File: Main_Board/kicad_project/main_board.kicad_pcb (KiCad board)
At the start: 4 copper layers, 150 x 150 mm, 237 parts, among them J1 MOTOR, J10 USB_B_Micro, J11 DATA_UART, J12 I2C_EXTERNAL, J13 DEBUG_HEADER, J14 IO1, J15 IO7, J16 IO2, J17 IO3, J18 IO8, J19 IO9, J2 MOTOR, J20 IO4, J21 IO5, J22 IO10, J23 IO6, J24 EXPANSION_HEADER, J3 MOTOR, J4 MOTOR, J5 PWR_ENTRY, J6 12V_HDR, J7 3V3_HDR, J8 5V_HDR, J9 I2C_BUFFERED, SW1 SW_SPST, U1 TMC2209, U2 TMC2209, U3 TMC2209, U4 TMC2209, U5 TPS562200, U6 TPS562200, U7 PCA9600DP, U8 USBLC6-2SC6, U9 STM32G474VxT, Y1 ABS06-32.768kHz, Y2 DNP

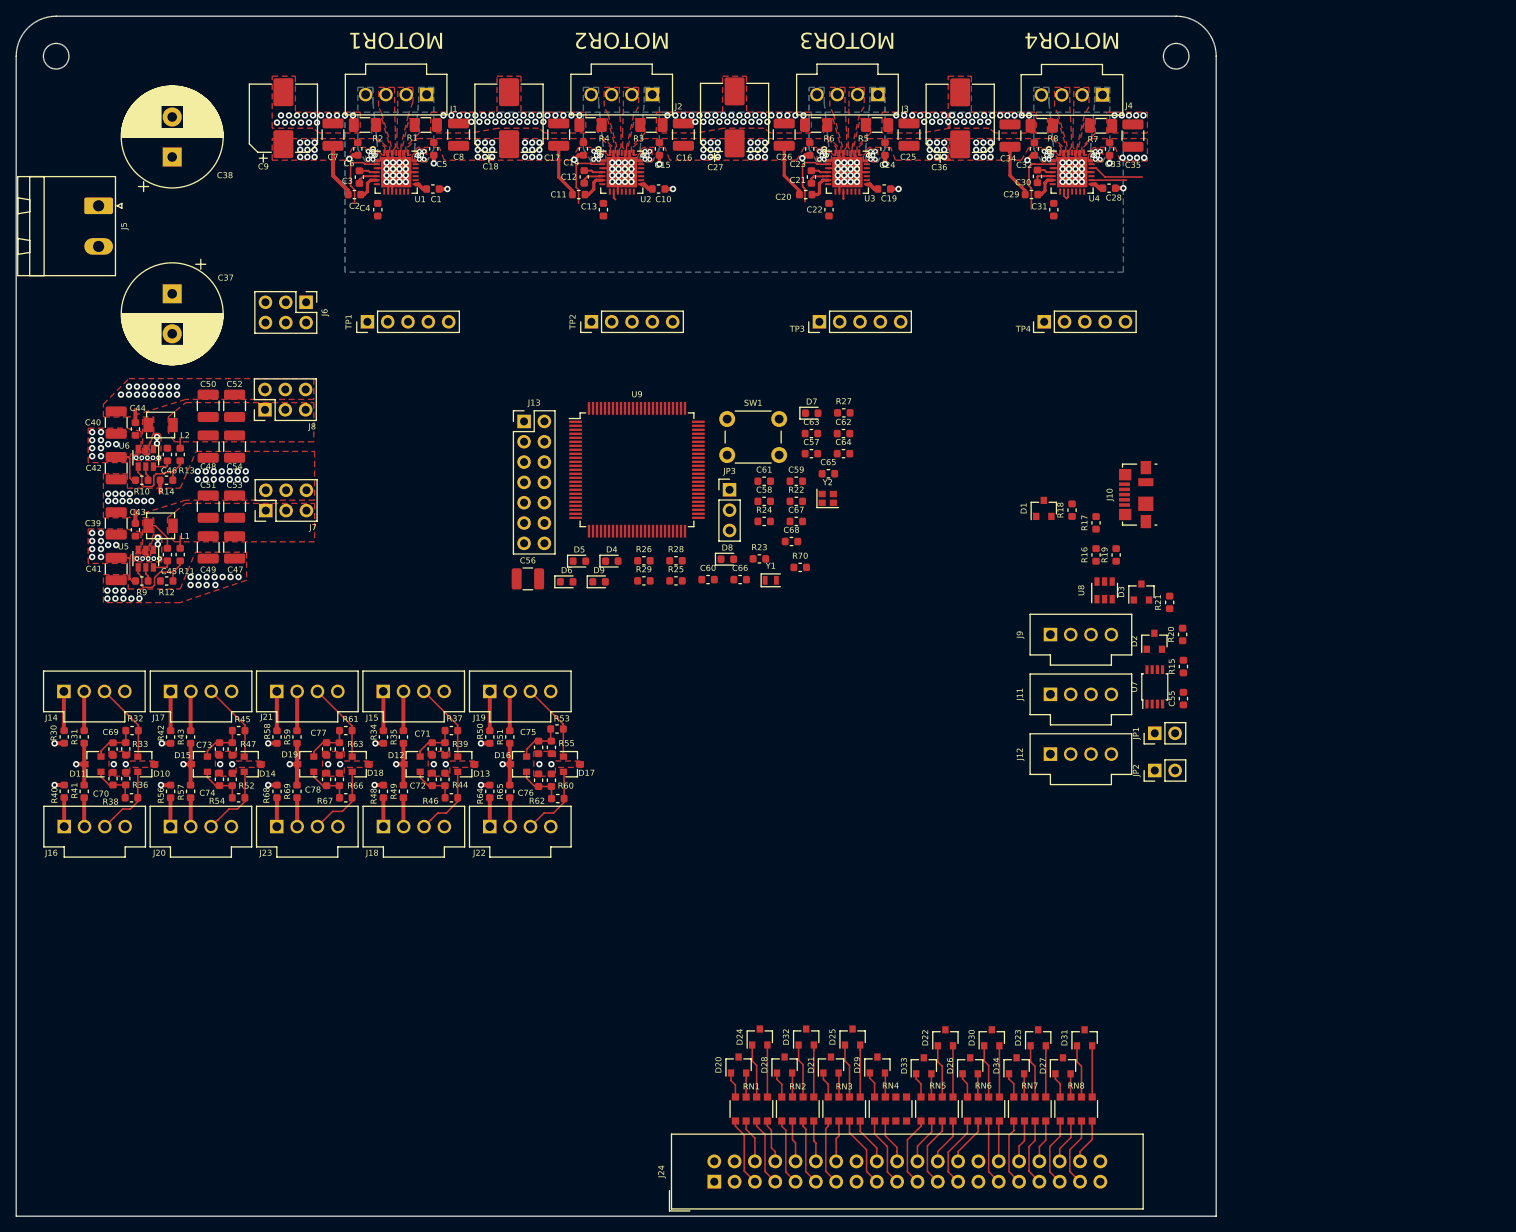
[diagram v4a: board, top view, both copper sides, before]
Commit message: external IO layout WIP, small chances to external IO schematic
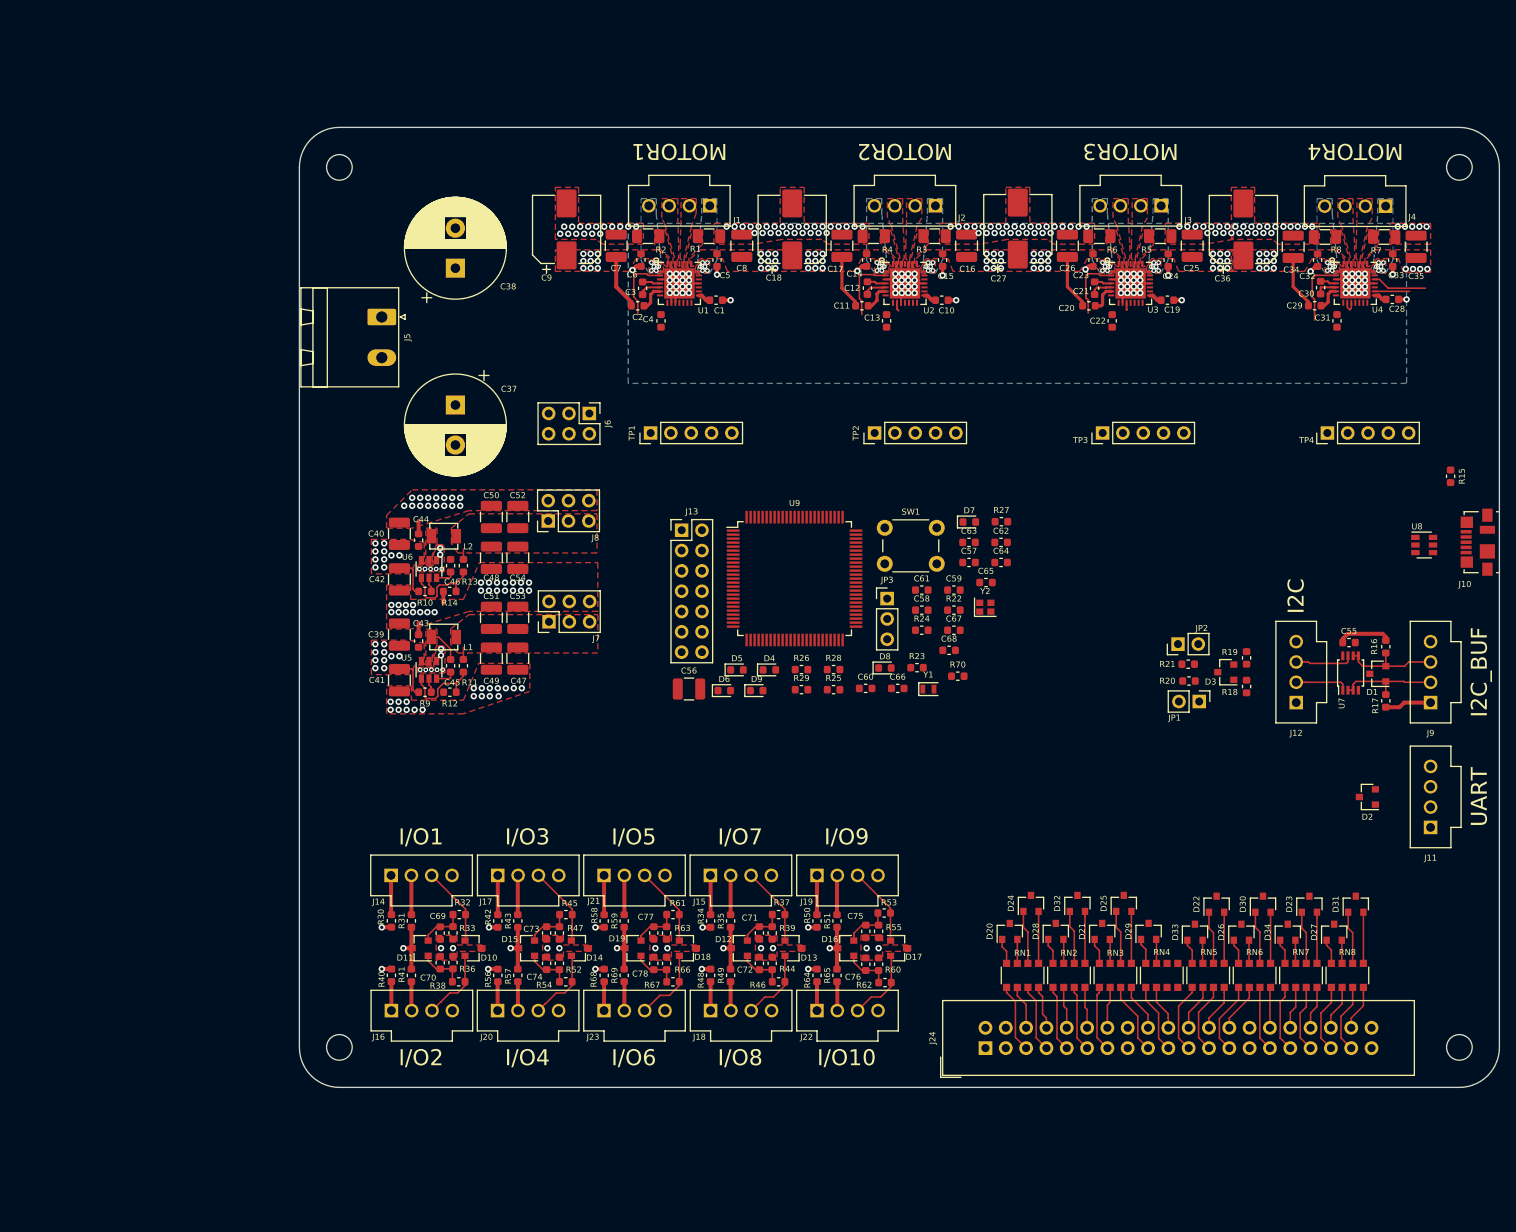
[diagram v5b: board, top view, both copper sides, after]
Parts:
- added REF**: MountingHole_3.2mm_M3, MountingHole:MountingHole_3.2mm_M3, F.Cu at (203.4, 148.9)
- added REF**: MountingHole_3.2mm_M3, MountingHole:MountingHole_3.2mm_M3, F.Cu at (63.4, 148.9)
- R15: value 33K -> 1M
- moved J11 50.3 mm to (199.8, 121.4), turned to 180 degrees
- moved J9 48.3 mm to (199.8, 105.8), turned to 180 degrees
- moved C69 46.9 mm to (76.0, 134.6)
- moved J16 46.9 mm to (69.9, 144.3)
- moved J20 46.9 mm to (83.2, 144.3)
- moved J23 46.9 mm to (96.5, 144.3)
- moved R32 46.9 mm to (78.4, 132.3)
- moved R45 46.9 mm to (91.7, 132.3)
- moved J18 46.9 mm to (109.8, 144.3)
- moved J22 46.9 mm to (123.1, 144.3)
- moved R36 46.9 mm to (77.6, 138.3)
- moved R37 46.9 mm to (118.3, 132.3)
- moved R61 46.9 mm to (105.1, 132.3)
- moved R62 46.9 mm to (131.6, 140.8)
- moved C70 46.9 mm to (76.0, 138.3)
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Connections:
- J12 pad 2: Net-(D3-Pad2) -> Net-(D3-Pad1)
- J12 pad 3: Net-(D3-Pad1) -> Net-(D3-Pad2)
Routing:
- net Net-(D1-Pad1): track 0.00 -> 12.9 mm
- net +12V: track 48.7 -> 61.3 mm
- net Net-(D1-Pad2): track 0.00 -> 12.5 mm
- net Net-(D3-Pad2): track 0.00 -> 7.38 mm
- net Net-(D3-Pad1): track 0.00 -> 6.67 mm
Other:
- board size 150 x 150 mm -> 150 x 120 mm
- board text added: "I/O1"
- board text added: "I/O10"
- board text added: "I/O2"
- board text added: "I/O3"
- board text added: "I/O4"
- board text added: "I/O5"
- board text added: "I/O6"
- board text added: "I/O7"
- board text added: "I/O8"
- board text added: "I/O9"
- board text added: "I2C"
- board text added: "I2C_BUF"
- board text added: "UART"

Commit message: routing half finished
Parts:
- moved C56 47.5 mm to (150.8, 85.4), turned to 90 degrees
- moved J13 40.9 mm to (147.1, 84.0), turned to 270 degrees
- moved SW1 34.6 mm to (103.0, 103.4)
- moved C63 28.8 mm to (139.5, 114.5)
- moved C68 28.1 mm to (111.9, 104.2), turned to 90 degrees
- moved C62 27.8 mm to (140.3, 113.0)
- moved R22 27.5 mm to (114.3, 103.4)
- moved D7 25.2 mm to (117.1, 85.9)
- moved R27 24.6 mm to (121.7, 85.9)
- moved U9 24.3 mm to (141.3, 102.6)
- moved C60 24.0 mm to (151.7, 95.8), turned to 90 degrees
- moved C64 22.6 mm to (125.5, 97.7)
- moved C57 22.6 mm to (130.9, 107.9), turned to 270 degrees
- moved R25 22.0 mm to (121.7, 82.5)
- moved R24 21.6 mm to (121.7, 80.8)
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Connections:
- net /External I/O/USB_DM renamed /External I/O/USB_DATA_N
- net /External I/O/USB_DP renamed /External I/O/USB_DATA_P
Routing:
- net +3V3: track 43.5 -> 190.4 mm, vias 5 -> 20
- net /STEP1/ENABLE: track 8.49 -> 139.4 mm, vias 0 -> 2
- net /STEP1/STEP: track 0.00 -> 127.3 mm, vias 0 -> 2
- net /STEP1/DIAG: track 0.00 -> 124.7 mm, vias 0 -> 2
- net GND: track 46.6 -> 161.3 mm, vias 263 -> 335
- net /STEP4/STEP: track 4.38 -> 110.8 mm, vias 0 -> 2
- net /STEP2/ENABLE: track 8.32 -> 112.4 mm, vias 0 -> 2
- net /STEP1/DIR: track 0.00 -> 100.2 mm, vias 0 -> 2
- net /MCU/STEP_UART_RX: track 0.00 -> 97.3 mm, vias 0 -> 1
- net /STEP2/DIAG: track 0.00 -> 96.7 mm, vias 0 -> 2
- net /STEP4/DIR: track 6.81 -> 93.7 mm, vias 0 -> 2
- net /Limit Switches/IO2: track 5.80 -> 92.2 mm, vias 0 -> 2
- net /STEP2/STEP: track 0.00 -> 85.7 mm, vias 0 -> 2
- net /STEP4/DIAG: track 0.00 -> 83.0 mm, vias 0 -> 2
- net /STEP4/ENABLE: track 8.46 -> 86.5 mm, vias 0 -> 2
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- added copper zone on F.Cu, net Net-(J10-Pad6)
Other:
- board text added: "12V SDA SCL GND"
- board text added: "3V3"
- board text added: "3V3 SDA SCL GND"
- board text added: "3V3 TX RX GND"
- board text added: "Always: 12V 3V3 I/O GND"
- board text added: "BOOT0"
- board text added: "DEBUG"
- board text added: "GND"
- board text added: "LED1 LED2 LED3 LED4 LED5 LED6"
- board text added: "RESET"

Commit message: routing finished
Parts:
- moved C60 1.58 mm to (150.2, 95.3), turned to 180 degrees
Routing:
- net /MCU/STEP_UART_RX: track 97.3 -> 231.2 mm
- net /MCU/EXP_IO28: track 2.92 -> 86.1 mm, vias 0 -> 2
- net /MCU/EXP_IO30: track 6.40 -> 89.5 mm, vias 0 -> 2
- net /MCU/EXP_IO27: track 3.15 -> 85.5 mm, vias 0 -> 2
- net /MCU/EXP_IO29: track 6.63 -> 88.0 mm, vias 0 -> 2
- net /MCU/EXP_IO26: track 6.40 -> 83.4 mm, vias 0 -> 2
- net /MCU/EXP_IO25: track 6.63 -> 81.3 mm, vias 0 -> 2
- net /MCU/EXP_IO23: track 3.15 -> 75.3 mm, vias 0 -> 2
- net /MCU/EXP_IO18: track 6.40 -> 78.3 mm, vias 0 -> 2
- net /MCU/EXP_IO24: track 2.92 -> 74.7 mm, vias 0 -> 2
- net /MCU/EXP_IO16: track 2.92 -> 71.0 mm, vias 0 -> 2
- net /MCU/EXP_IO17: track 6.63 -> 72.4 mm, vias 0 -> 2
- net /MCU/EXP_IO15: track 3.15 -> 68.7 mm, vias 0 -> 2
- net /External I/O/DATA_UART_TX: track 6.13 -> 69.8 mm, vias 0 -> 2
- net /External I/O/DATA_UART_RX: track 6.14 -> 67.8 mm, vias 0 -> 2
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- added copper zone on In1.Cu, net GND

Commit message: add graphics
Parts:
- added G***: LOGO, LoaDy:FI_LOGO_15x14mm, F.Cu at (162.8, 89.8)
- added G***: LOGO, LoaDy:EmLab_LOGO_13mm, F.Cu at (167.3, 120.6)
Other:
- board text added: "Cube Main Board"
- board text added: "Cube Main Board Revision 1 O. Pecák (LoaDy) September 2020"
